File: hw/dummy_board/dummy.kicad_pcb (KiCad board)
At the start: 2 copper layers, 29.8 x 40.6 mm, 11 parts, among them J1 Conn_02x04, J2 FFC, U1 W25Q128JVS, U2 W25Q128JVS, U3 W25Q128JVP, U4 W25Q128JVS

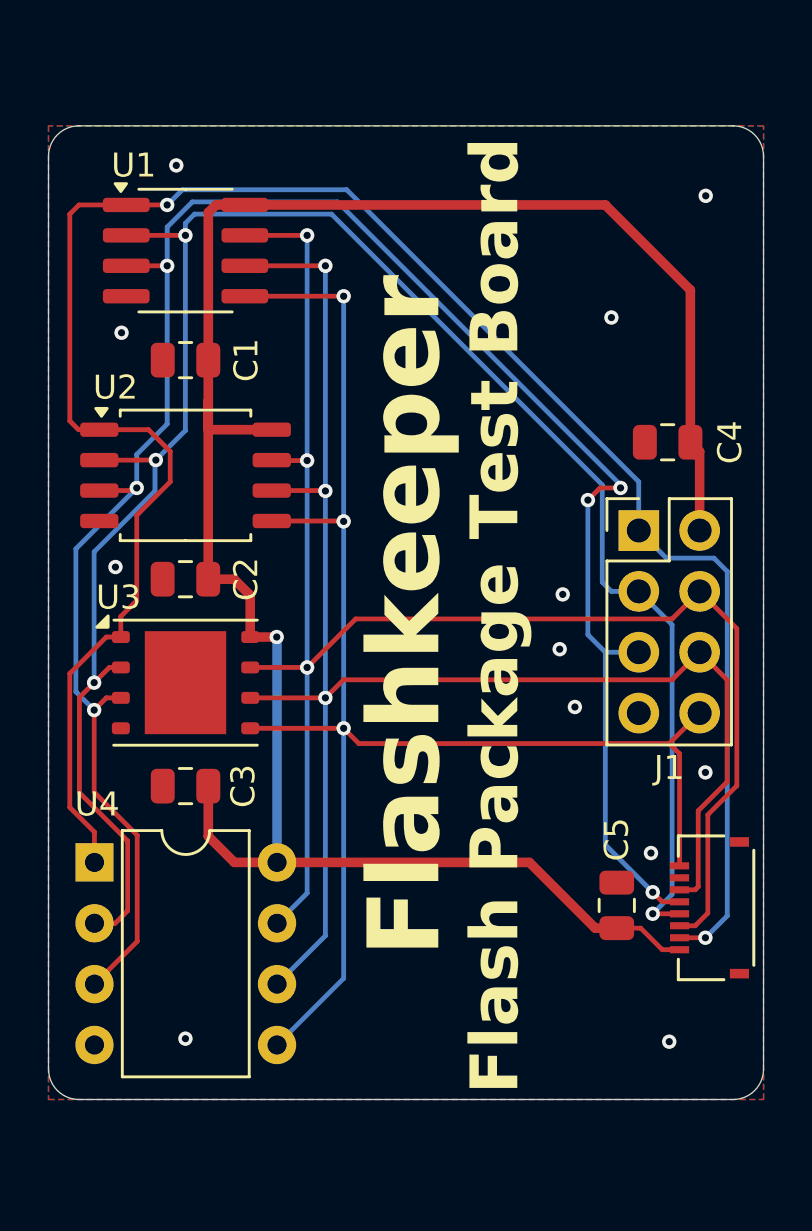
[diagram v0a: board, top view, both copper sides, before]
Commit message: Add KiCAD source for Flashkeeper FPGA SoM and its production panel and its associated component libraries. Add basic 3D models for some of the chip packages used. Minimal initial PicoSoC/PicoRV32 configuration and firmware for FPGA SoM bringup. Update gitignores.
Signed-off-by: Dodoid <git-noreply@dodoid.com>
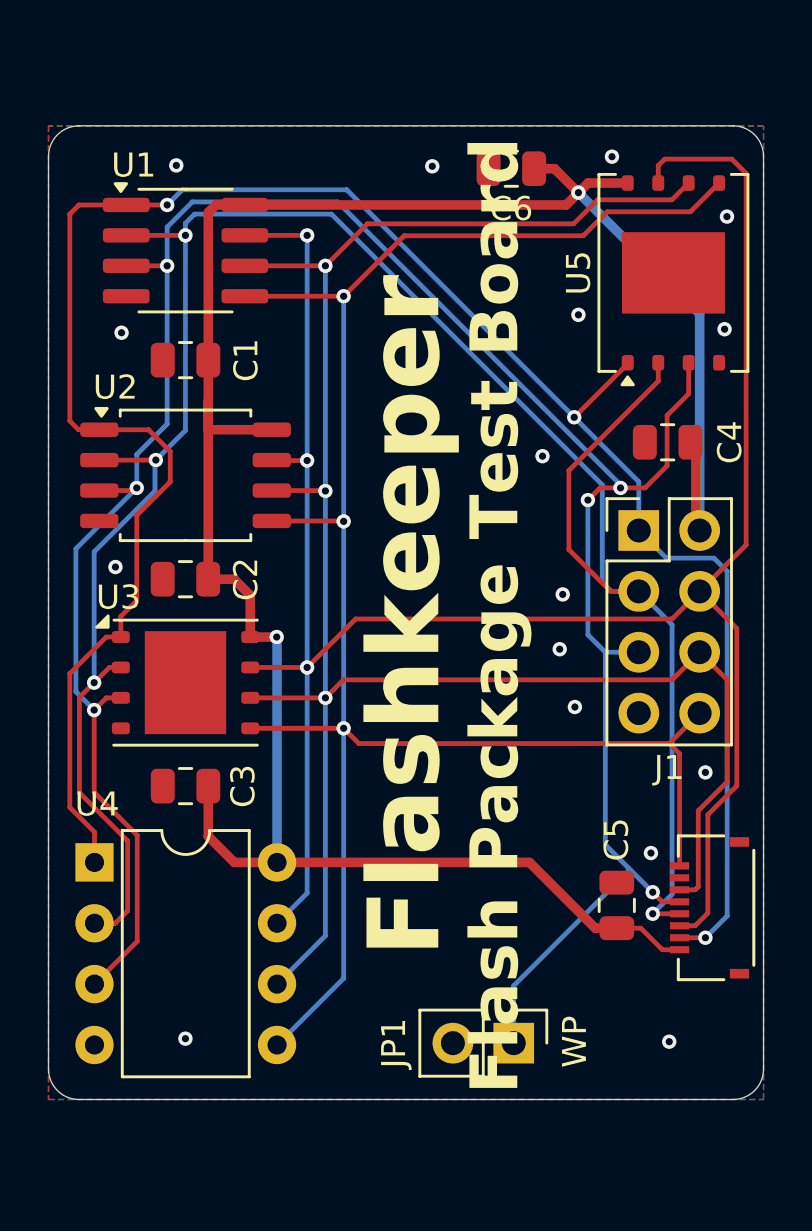
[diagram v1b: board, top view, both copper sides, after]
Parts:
- added C6: 0.1uF, Capacitor_SMD:C_0805_2012Metric, F.Cu at (172.1, 72.4)
- added JP1: Jumper_2_Open, Connector_PinHeader_2.54mm:PinHeader_1x02_P2.54mm_Vertical, F.Cu at (172.2, 108.9)
- added U5: W25Q128JVP, Package_SON:WSON-8-1EP_8x6mm_P1.27mm_EP3.4x4.3mm, F.Cu at (178.9, 76.8)
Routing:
- net IO3: track 69.4 -> 92.4 mm
- net DI: track 64.4 -> 82.0 mm
- net CLK: track 67.6 -> 84.2 mm
- net IO2: track 85.7 -> 102.0 mm
- net DO: track 82.6 -> 95.6 mm
- net VCC: track 89.1 -> 97.5 mm, vias 1 -> 2
- net CS: track 85.4 -> 88.6 mm, vias 2 -> 3
- net GND: vias 13 -> 17
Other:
- board text added: "WP"
